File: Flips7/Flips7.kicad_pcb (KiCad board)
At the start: 2 copper layers, 100 x 100 mm, 16 parts, among them CN1 Conn_02x17_Odd_Even, CN2 Conn_02x17_Odd_Even, U1 FP2800A, U2 FP2800A, U3 FP2800A

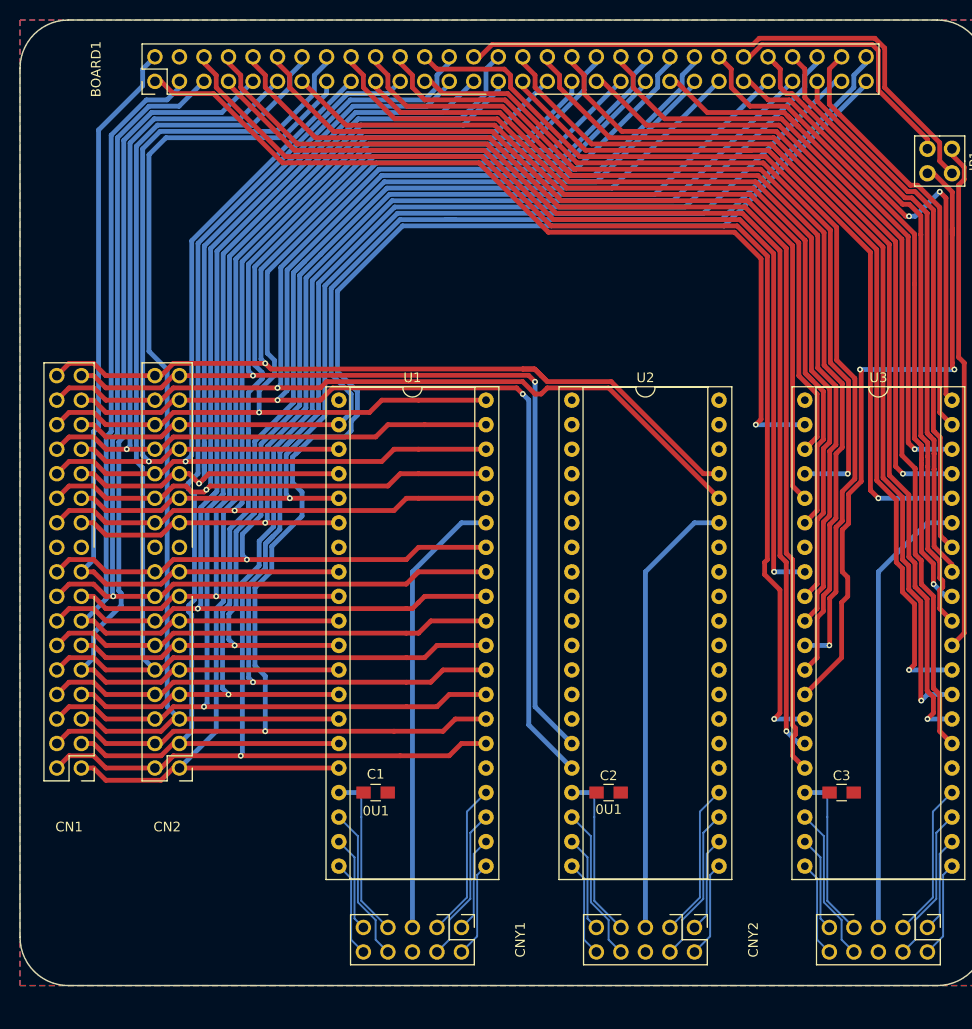
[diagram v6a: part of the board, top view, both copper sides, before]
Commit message: Fixing C values to 0µ1; connecting VCC of 3 units
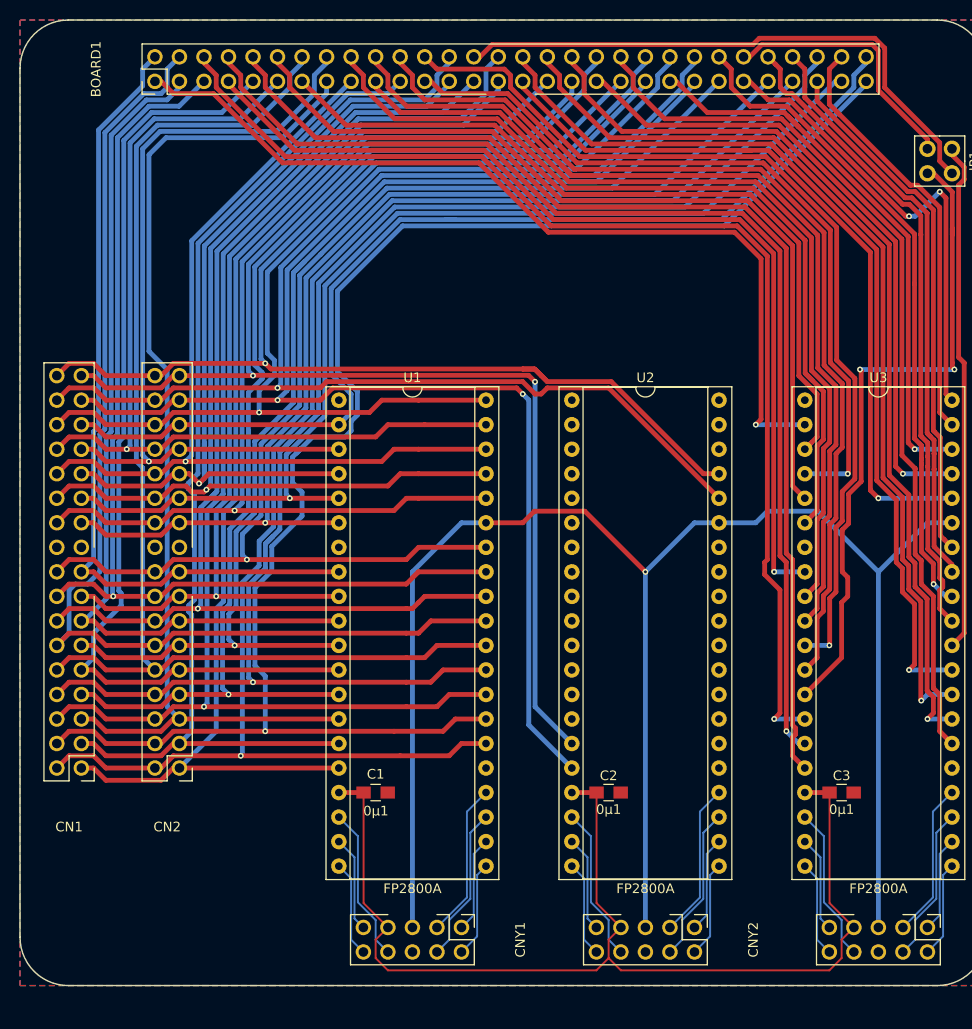
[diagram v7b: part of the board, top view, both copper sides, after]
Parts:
- C1, C2, C3: value 0U1 -> 0µ1
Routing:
- net /RY12: track 46.6 -> 114.6 mm
- net /VCC: track 53.2 -> 114.1 mm
- net /HV: track 139.7 -> 178.9 mm, vias 0 -> 1
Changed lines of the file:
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@@
     (thickness 1.6)
     (drawings 20)
-    (tracks 1162)
+    (tracks 1190)
     (zones 0)
     (modules 16)
@@
       (effects (font (size 1 1) (thickness 0.15)))
     )
-    (fp_text value 0U1 (at 0 1.75) (layer F.SilkS)
+    (fp_text value 0µ1 (at 0 1.75) (layer F.SilkS)
       (effects (font (size 1 1) (thickness 0.15)))
     )
@@
       (effects (font (size 1 1) (thickness 0.15)))
     )
-    (fp_text value FP2800A (at 7.62 50.59) (layer F.Fab)
+    (fp_text value FP2800A (at 7.62 50.59) (layer F.SilkS)
       (effects (font (size 1 1) (thickness 0.15)))
     )
@@
       (effects (font (size 1 1) (thickness 0.15)))
     )
-    (fp_text value FP2800A (at 7.62 50.59) (layer F.Fab)
+    (fp_text value FP2800A (at 7.62 50.59) (layer F.SilkS)
       (effects (font (size 1 1) (thickness 0.15)))
     )
@@
       (effects (font (size 1 1) (thickness 0.15)))
     )
-    (fp_text value 0U1 (at 0 1.75) (layer F.Fab)
+    (fp_text value 0µ1 (at 0 1.75) (layer F.SilkS)
       (effects (font (size 1 1) (thickness 0.15)))
     )
@@
       (effects (font (size 1 1) (thickness 0.15)))
     )
-    (fp_text value FP2800A (at 7.62 50.59) (layer F.Fab)
+    (fp_text value FP2800A (at 7.62 50.59) (layer F.SilkS)
       (effects (font (size 1 1) (thickness 0.15)))
     )
@@
       (effects (font (size 1 1) (thickness 0.15)))
     )
-    (fp_text value 0U1 (at -0.02 -1.905 180) (layer F.SilkS)
+    (fp_text value 0µ1 (at -0.02 -1.905 180) (layer F.SilkS)
       (effects (font (size 1 1) (thickness 0.15)))
     )
@@
   (segment (start 65.405 88.9) (end 66.675 88.9) (width 0.5) (layer F.Cu) (net 100))
   (segment (start 66.675 88.9) (end 67.945 87.63) (width 0.5) (layer F.Cu) (net 100))
+  (segment (start 41.91 29.21) (end 40.64 30.48) (width 0.5) (layer B.Cu) (net 100) (status 400000))
+  (segment (start 30.48 88.9) (end 29.21 90.17) (width 0.5) (layer B.Cu) (net 100) (status 800000))
+  (segment (start 30.48 84.455) (end 30.48 88.9) (width 0.5) (layer B.Cu) (net 100))
+  (segment (start 31.115 83.82) (end 30.48 84.455) (width 0.5) (layer B.Cu) (net 100))
+  (segment (start 32.385 83.82) (end 31.115 83.82) (width 0.5) (layer B.Cu) (net 100))
+  (segment (start 33.672402 82.532598) (end 32.385 83.82) (width 0.5) (layer B.Cu) (net 100))
+  (segment (start 33.672402 68.282484) (end 33.672402 82.532598) (width 0.5) (layer B.Cu) (net 100))
+  (segment (start 34.185588 67.769298) (end 33.672402 68.282484) (width 0.5) (layer B.Cu) (net 100))
+  (segment (start 34.185588 37.053868) (end 34.185588 67.769298) (width 0.5) (layer B.Cu) (net 100))
+  (segment (start 38.219456 33.02) (end 34.185588 37.053868) (width 0.5) (layer B.Cu) (net 100))
+  (segment (start 40.005 33.02) (end 38.219456 33.02) (width 0.5) (layer B.Cu) (net 100))
+  (segment (start 40.64 32.385) (end 40.005 33.02) (width 0.5) (layer B.Cu) (net 100))
+  (segment (start 40.64 30.48) (end 40.64 32.385) (width 0.5) (layer B.Cu) (net 100))
   (segment (start 29.21 92.71) (end 30.48 91.44) (width 0.5) (layer F.Cu) (net 101) (status 400010))
   (segment (start 34.29 92.71) (end 39.37 92.71) (width 0.5) (layer F.Cu) (net 101) (status 20))
@@
   (segment (start 57.624118 53.191238) (end 57.624118 62.069118) (width 0.5) (layer B.Cu) (net 110))
   (segment (start 64.747316 46.06804) (end 57.624118 53.191238) (width 0.5) (layer B.Cu) (net 110))
-  (segment (start 111.76 119.38) (end 109.007206 116.627206) (width 0.2) (layer B.Cu) (net 111) (status 400010))
-  (segment (start 109.007206 116.627206) (end 109.007206 107.95) (width 0.2) (layer B.Cu) (net 111))
-  (segment (start 87.63 119.38) (end 84.877206 116.627206) (width 0.2) (layer B.Cu) (net 111) (status 400010))
-  (segment (start 84.877206 116.627206) (end 84.877206 107.95) (width 0.2) (layer B.Cu) (net 111))
-  (segment (start 63.5 119.38) (end 60.747206 116.627206) (width 0.2) (layer B.Cu) (net 111) (status 400010))
-  (segment (start 60.747206 116.627206) (end 60.747206 107.95) (width 0.2) (layer B.Cu) (net 111))
-  (segment (start 109.007206 107.95) (end 109.007206 105.622794) (width 0.2) (layer B.Cu) (net 111))
-  (segment (start 109.22 105.41) (end 106.68 105.41) (width 0.5) (layer B.Cu) (net 111) (status 800000))
-  (segment (start 109.007206 105.622794) (end 109.22 105.41) (width 0.2) (layer B.Cu) (net 111))
-  (segment (start 84.877206 107.95) (end 84.877206 105.622794) (width 0.2) (layer B.Cu) (net 111))
-  (segment (start 85.09 105.41) (end 82.55 105.41) (width 0.5) (layer B.Cu) (net 111) (status 800000))
-  (segment (start 84.877206 105.622794) (end 85.09 105.41) (width 0.2) (layer B.Cu) (net 111))
-  (segment (start 60.747206 107.95) (end 60.747206 105.622794) (width 0.2) (layer B.Cu) (net 111))
-  (segment (start 60.96 105.41) (end 58.42 105.41) (width 0.5) (layer B.Cu) (net 111) (status 800000))
-  (segment (start 60.747206 105.622794) (end 60.96 105.41) (width 0.2) (layer B.Cu) (net 111))
+  (segment (start 109.22 105.41) (end 106.68 105.41) (width 0.5) (layer F.Cu) (net 111) (status 800000))
+  (segment (start 85.09 105.41) (end 82.55 105.41) (width 0.5) (layer F.Cu) (net 111) (status 800000))
+  (segment (start 60.96 105.41) (end 58.42 105.41) (width 0.5) (layer F.Cu) (net 111) (status 800000))
+  (segment (start 109.24 116.86) (end 109.24 105.41) (width 0.2) (layer F.Cu) (net 111))
+  (segment (start 111.76 119.38) (end 109.24 116.86) (width 0.2) (layer F.Cu) (net 111))
+  (segment (start 87.63 119.38) (end 85.11 116.86) (width 0.2) (layer F.Cu) (net 111) (status 400000))
+  (segment (start 85.11 116.86) (end 85.11 105.41) (width 0.2) (layer F.Cu) (net 111) (status 800000))
+  (segment (start 63.5 119.38) (end 60.98 116.86) (width 0.2) (layer F.Cu) (net 111) (status 400000))
+  (segment (start 60.98 116.86) (end 60.98 105.41) (width 0.2) (layer F.Cu) (net 111) (status 800000))
+  (segment (start 63.5 119.38) (end 62.23 120.65) (width 0.2) (layer F.Cu) (net 111) (status 400000))
+  (segment (start 86.36 120.65) (end 87.63 119.38) (width 0.2) (layer F.Cu) (net 111) (status 800000))
+  (segment (start 86.36 122.555) (end 86.36 120.65) (width 0.2) (layer F.Cu) (net 111))
+  (segment (start 85.09 123.825) (end 86.36 122.555) (width 0.2) (layer F.Cu) (net 111))
+  (segment (start 63.5 123.825) (end 85.09 123.825) (width 0.2) (layer F.Cu) (net 111))
+  (segment (start 62.23 122.555) (end 63.5 123.825) (width 0.2) (layer F.Cu) (net 111))
+  (segment (start 62.23 120.65) (end 62.23 122.555) (width 0.2) (layer F.Cu) (net 111))
+  (segment (start 86.36 122.555) (end 87.63 123.825) (width 0.2) (layer F.Cu) (net 111))
+  (segment (start 110.49 120.65) (end 111.76 119.38) (width 0.2) (layer F.Cu) (net 111) (status 800000))
+  (segment (start 110.49 122.555) (end 110.49 120.65) (width 0.2) (layer F.Cu) (net 111))
+  (segment (start 109.22 123.825) (end 110.49 122.555) (width 0.2) (layer F.Cu) (net 111))
+  (segment (start 87.63 123.825) (end 109.22 123.825) (width 0.2) (layer F.Cu) (net 111))
   (segment (start 66.04 119.38) (end 66.04 82.55) (width 0.5) (layer B.Cu) (net 113) (status 10))
   (segment (start 71.12 77.47) (end 73.66 77.47) (width 0.5) (layer B.Cu) (net 113) (status 20))
@@
   (segment (start 119.38 77.47) (end 121.92 77.47) (width 0.5) (layer B.Cu) (net 113) (status 800020))
   (segment (start 114.3 82.55) (end 119.38 77.47) (width 0.5) (layer B.Cu) (net 113))
+  (segment (start 73.66 77.47) (end 77.47 77.47) (width 0.5) (layer F.Cu) (net 113))
+  (segment (start 78.672401 76.267599) (end 83.887599 76.267599) (width 0.5) (layer F.Cu) (net 113))
+  (segment (start 77.47 77.47) (end 78.672401 76.267599) (width 0.5) (layer F.Cu) (net 113))
+  (segment (start 83.887599 76.267599) (end 90.17 82.55) (width 0.5) (layer F.Cu) (net 113))
+  (via (at 90.17 82.55) (size 0.6) (drill 0.3) (layers F.Cu B.Cu) (net 113))
+  (segment (start 97.79 77.47) (end 101.6 77.47) (width 0.5) (layer B.Cu) (net 113))
+  (segment (start 108.017599 76.267599) (end 114.3 82.55) (width 0.5) (layer B.Cu) (net 113))
+  (segment (start 102.802401 76.267599) (end 108.017599 76.267599) (width 0.5) (layer B.Cu) (net 113))
+  (segment (start 101.6 77.47) (end 102.802401 76.267599) (width 0.5) (layer B.Cu) (net 113))
   (zone (net 112) (net_name /GND) (layer F.Cu) (hatch edge 0.508)
     (connect_pads (clearance 0.23))
